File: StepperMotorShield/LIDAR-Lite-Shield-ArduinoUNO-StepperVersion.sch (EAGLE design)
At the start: 10 parts

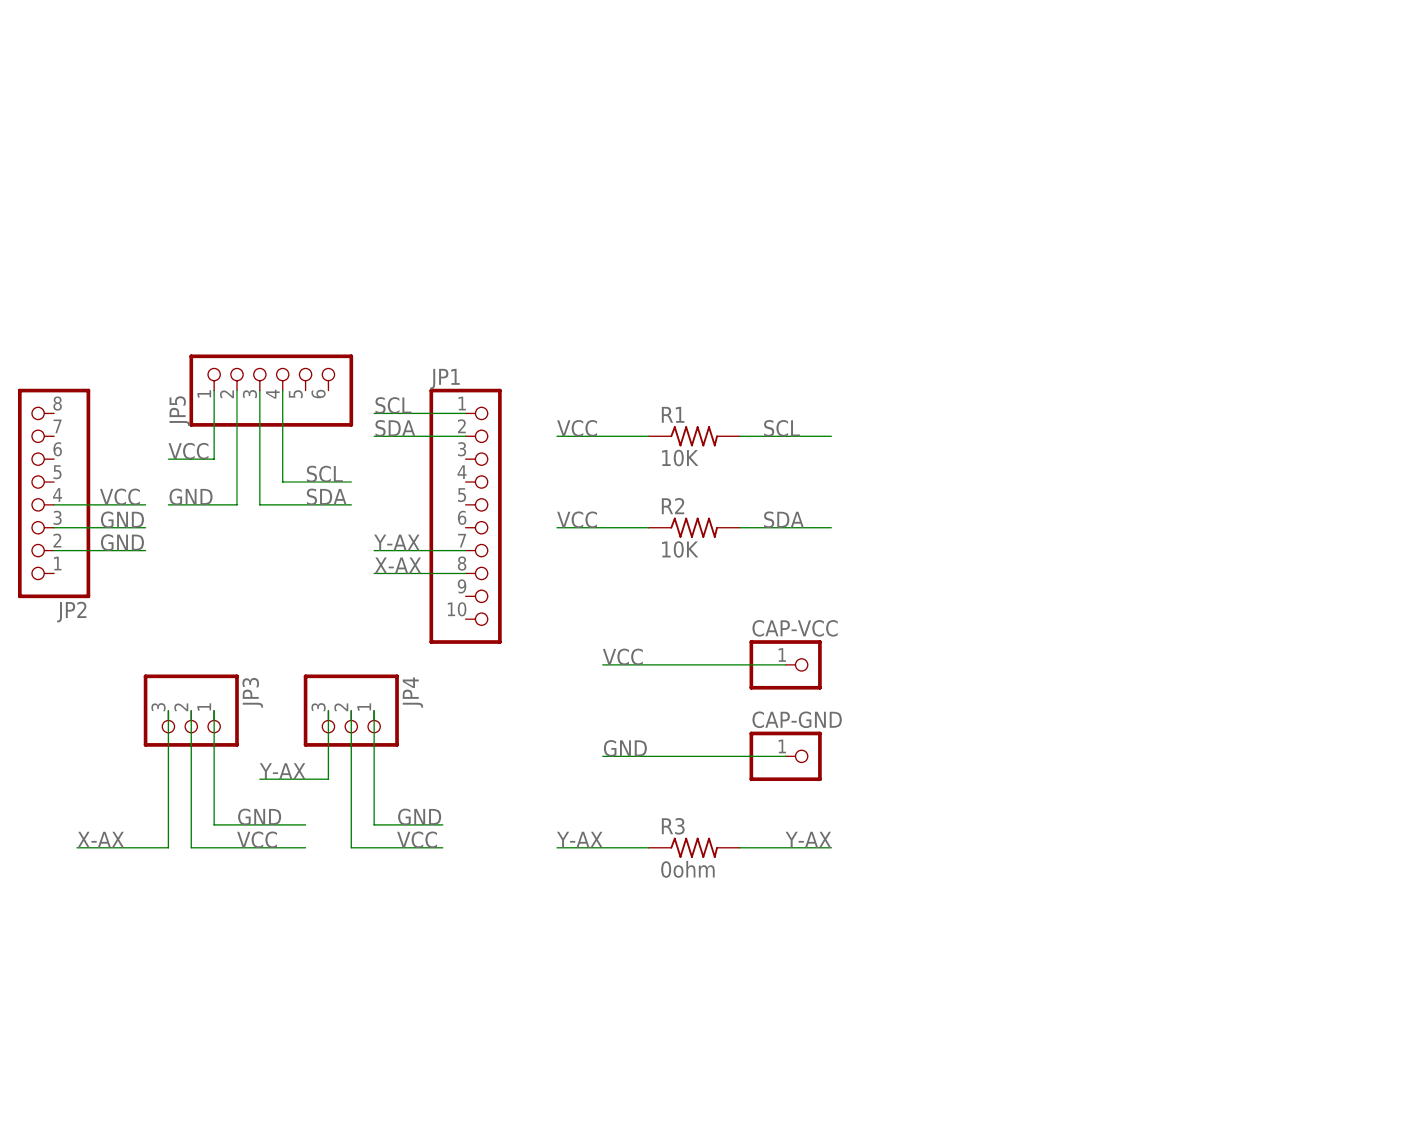
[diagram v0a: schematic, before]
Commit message: replace Stepper Motor Shiled PCB Design Files to Correct One
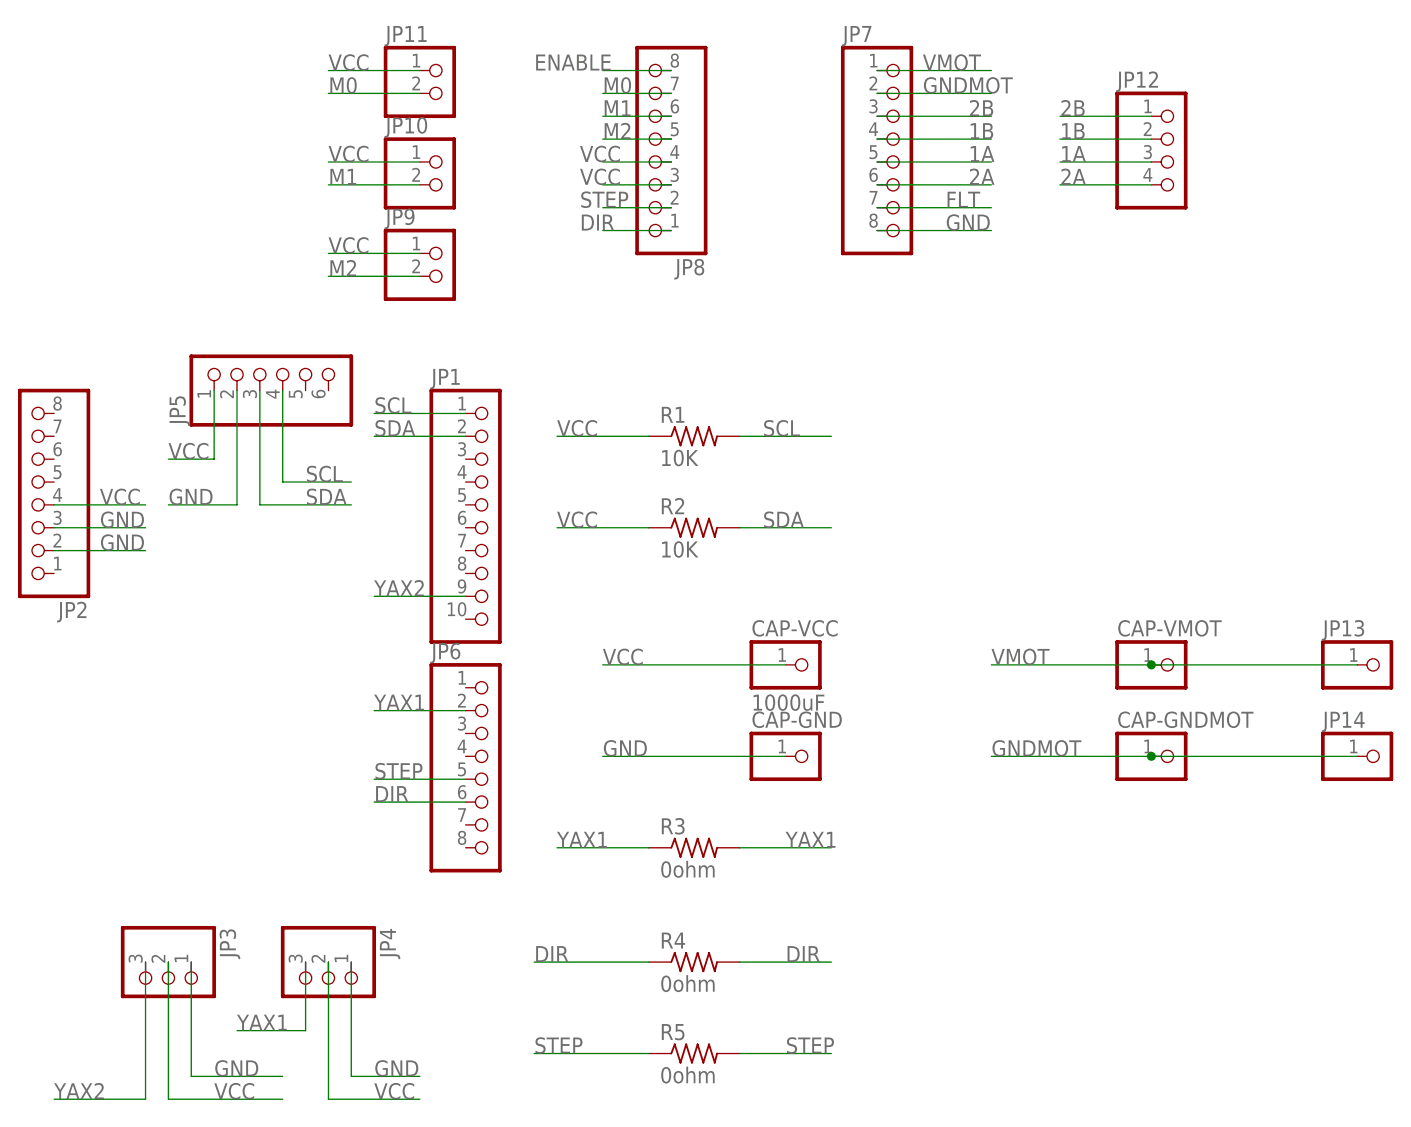
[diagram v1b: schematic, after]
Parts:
- added CAP-GNDMOT, CAP-VMOT, JP13, JP14: (no value), pinhead:PINHD-1X1
- added JP10, JP11, JP9: (no value), pinhead:PINHD-1X2
- added JP12: (no value), pinhead:PINHD-1X4
- added JP6, JP7, JP8: (no value), pinhead:PINHD-1X8
- added R4, R5: 0ohm, fab:RES-US1206FAB
- CAP-VCC: value (none) -> 1000uF
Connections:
- removed net X-AX: JP1.8, JP3.3
- removed net Y-AX: JP1.7, JP4.3, R3.1, R3.2
- new net 1A: JP12.3, JP7.5
- new net 1B: JP12.2, JP7.4
- new net 2A: JP12.4, JP7.6
- new net 2B: JP12.1, JP7.3
- new net DIR: JP6.6, JP8.1, R4.1, R4.2
- new net ENABLE: JP8.8
- new net FLT: JP7.7
- new net GNDMOT: CAP-GNDMOT.1, JP14.1, JP7.2
- new net M0: JP11.2, JP8.7
- new net M1: JP10.2, JP8.6
- new net M2: JP8.5, JP9.2
- new net STEP: JP6.5, JP8.2, R5.1, R5.2
- new net VMOT: CAP-VMOT.1, JP13.1, JP7.1
- new net YAX1: JP4.3, JP6.2, R3.1, R3.2
- new net YAX2: JP1.9, JP3.3
- net GND: now also JP7.8
- net VCC: now also JP10.1, JP11.1, JP8.3, JP8.4, JP9.1
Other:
- moved on the sheet: JP3, JP4
